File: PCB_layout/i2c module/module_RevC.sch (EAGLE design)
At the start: 86 parts, among them IC1 ATTINY85-20SU, J1 M20-9980346

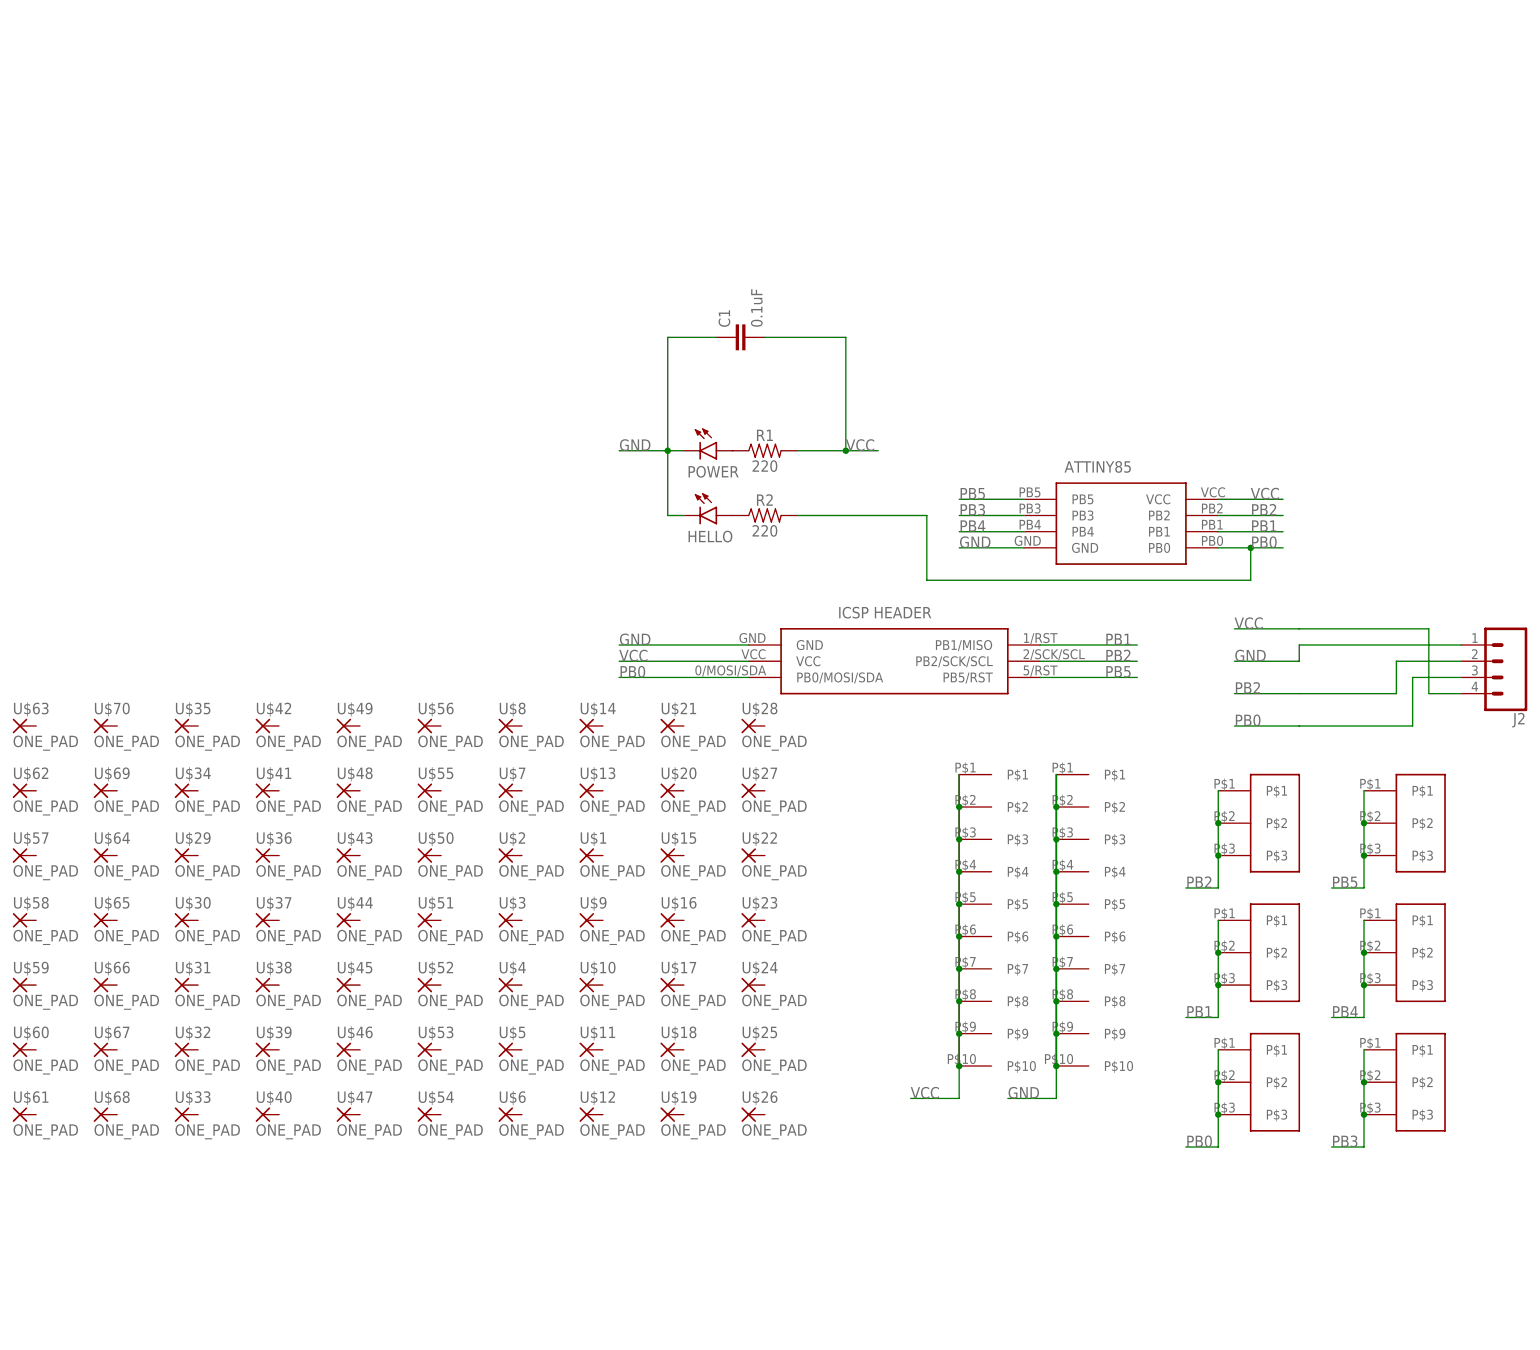
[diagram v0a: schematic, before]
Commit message: added i2c rev C
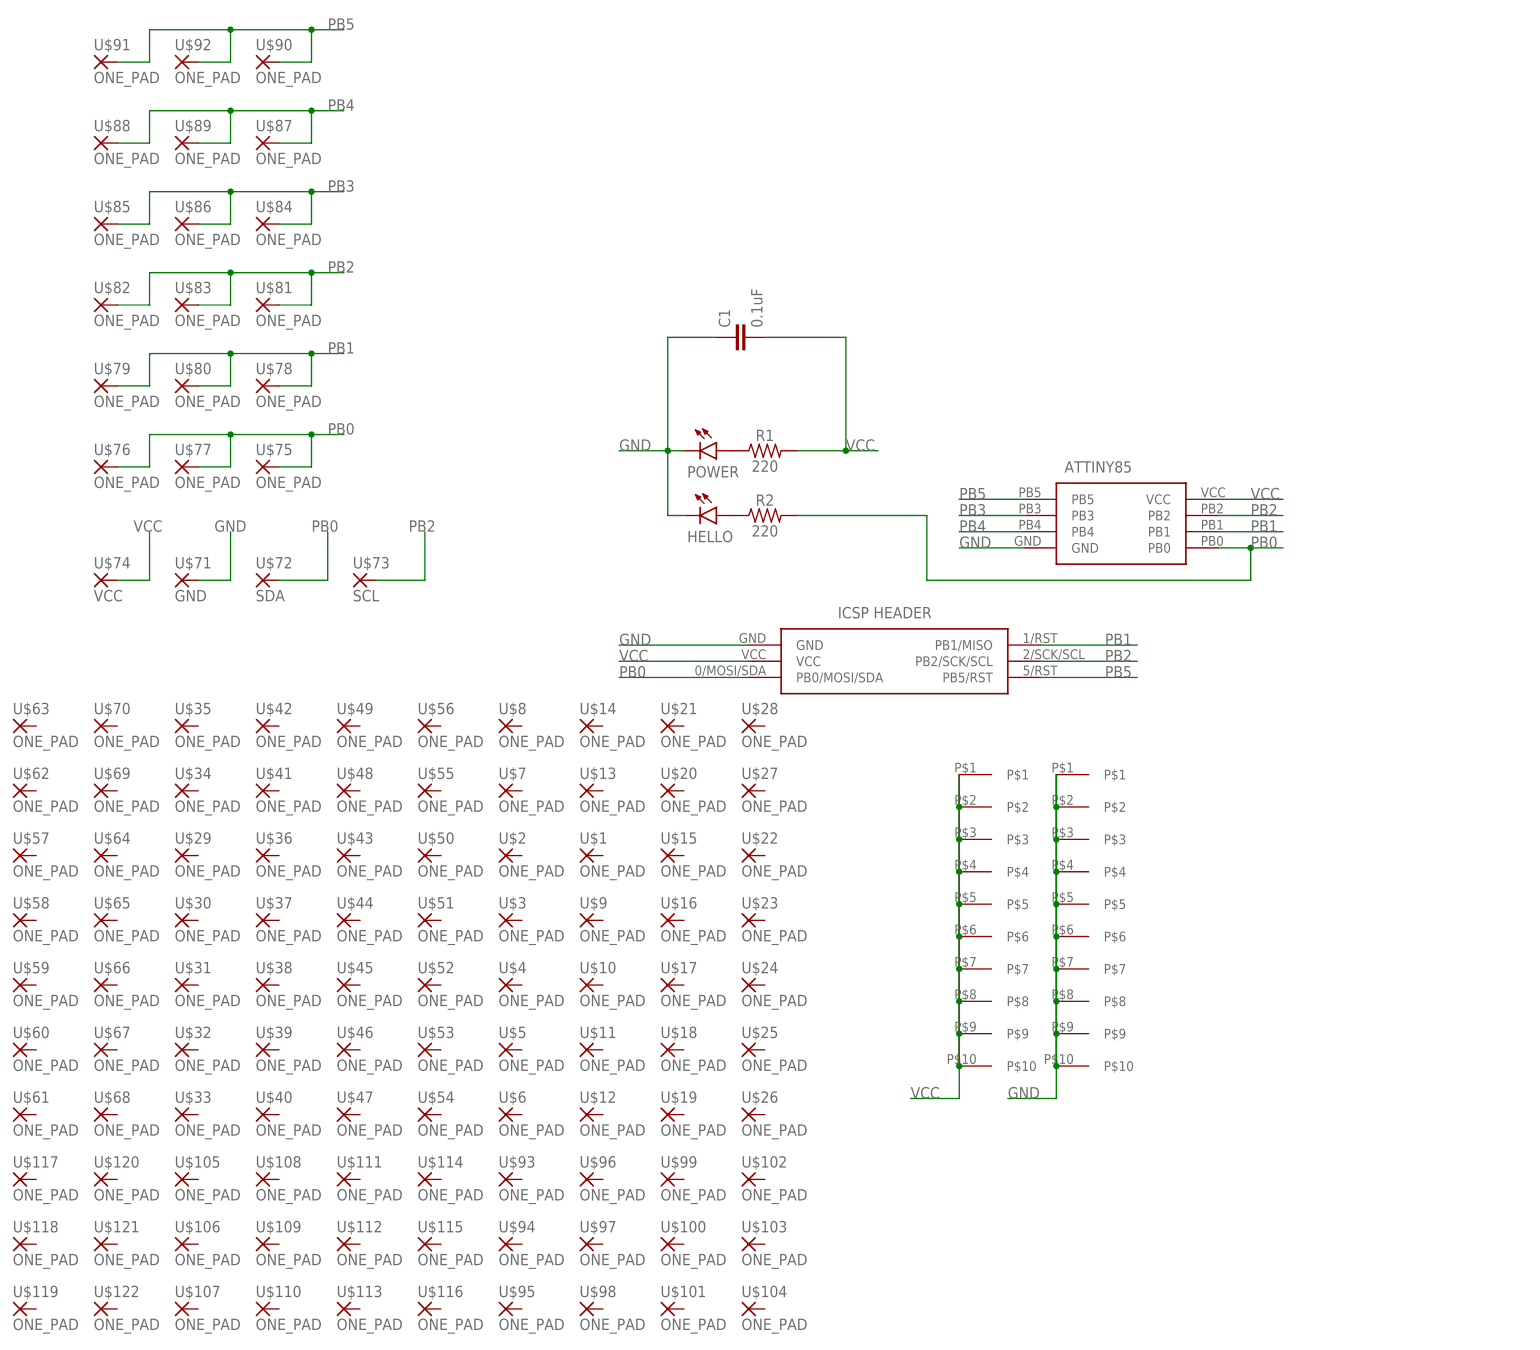
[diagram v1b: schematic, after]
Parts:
- removed 0, 1, 2, 3, 4, 5: 3X-PADS-CONNECTED, BadgeParts:3X-PADS-CONNECTED
- removed J2: (no value), SparkFun-Connectors:CONN_04
- added U$100, U$101, U$102, U$103, U$104, U$105, U$106, U$107, U$108, U$109, U$110, U$111, U$112, U$113, U$114, U$115, U$116, U$117, U$118, U$119, U$120, U$121, U$122, U$75, U$76, U$77, U$78, U$79, U$80, U$81, U$82, U$83, U$84, U$85, U$86, U$87, U$88, U$89, U$90, U$91, U$92, U$93, U$94, U$95, U$96, U$97, U$98, U$99: ONE_PAD, BadgeParts:ONE_PAD
- added U$71: GND, BadgeParts:ONE_PAD
- added U$72: SDA, BadgeParts:ONE_PAD
- added U$73: SCL, BadgeParts:ONE_PAD
- added U$74: VCC, BadgeParts:ONE_PAD
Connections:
- net GND: now also U$71.P; no longer J2.1
- net PB0: now also U$72.P, U$75.P, U$76.P, U$77.P; no longer 0.P$1, 0.P$2, 0.P$3, J2.3
- net PB1: now also U$78.P, U$79.P, U$80.P; no longer 1.P$1, 1.P$2, 1.P$3
- net PB2: now also U$73.P, U$81.P, U$82.P, U$83.P; no longer 2.P$1, 2.P$2, 2.P$3, J2.2
- net PB3: now also U$84.P, U$85.P, U$86.P; no longer 3.P$1, 3.P$2, 3.P$3
- net PB4: now also U$87.P, U$88.P, U$89.P; no longer 4.P$1, 4.P$2, 4.P$3
- net PB5: now also U$90.P, U$91.P, U$92.P; no longer 5.P$1, 5.P$2, 5.P$3
- net VCC: now also U$74.P; no longer J2.4

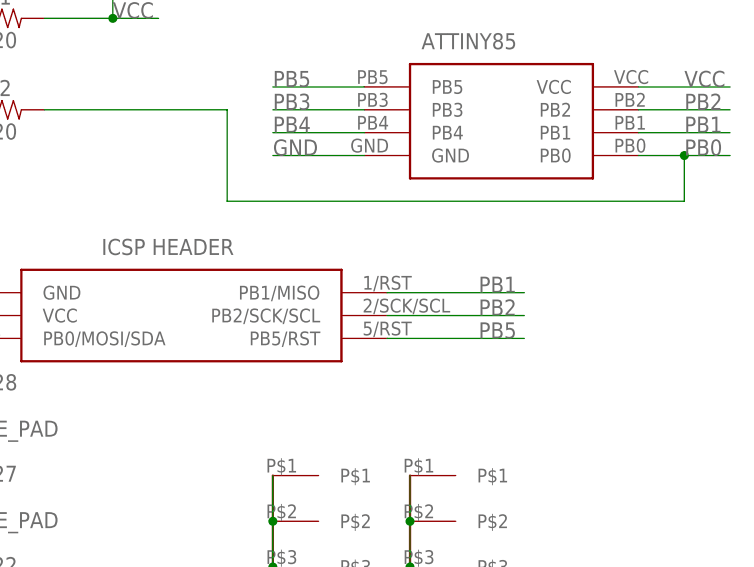
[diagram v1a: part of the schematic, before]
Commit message: fixed duplicate RST reference in ICSP definition
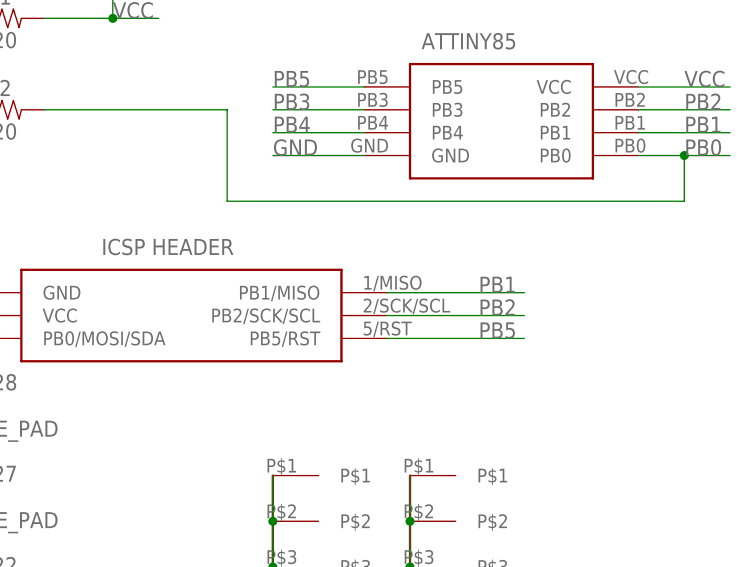
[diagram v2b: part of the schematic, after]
